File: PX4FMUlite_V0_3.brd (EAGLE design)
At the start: 48.6 x 34.9 mm, 152 parts, among them J2 DF13-4P-1.25V, J201 DF13C-6P-1.25V, J202 DF13C-6P-1.25V, J203 DF13C-6P-1.25V, J3 DF13C-4P-1.25V, J302 DF13C-4P-1.25V, J401 DF13C-4P-1.25V, J403 DF13C-7P-1.25V, J405 DF13C-4P-1.25V, J801 JST-ZH-3, J802 DF13C-3P-1.25V, M3_MOUNT1101 MOUNT-HOLE3.1MM, M3_MOUNT1102 MOUNT-HOLE3.1MM, M3_MOUNT1103 MOUNT-HOLE3.1MM, M3_MOUNT1104 MOUNT-HOLE3.1MM, U101 STM32F4X7VX, U2 MAX3051, U401 MAX3051, U903 74LVC2G240, X101 3.2x2.5 mm / 24 MHz / 15 ppm

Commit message: More tweaks
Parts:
- moved U$202 0.41 mm to (32.9, 7.52), turned to 180 degrees
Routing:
- net SERIAL2_TX: track 0.00 -> 6.91 mm
- net SERIAL2_RX: track 0.00 -> 5.37 mm
- net SERIAL2_CTS: track 0.00 -> 4.00 mm
- net 5V_S2_FILTERED: track 16.2 -> 18.7 mm
- net SERIAL2_RTS: track 0.00 -> 2.41 mm
- net VDD_5V_PERIPH: track 0.00 -> 2.28 mm, vias 0 -> 2
- net VDD_5V: track 14.7 -> 16.7 mm, vias 0 -> 4
- net N$5: track 0.00 -> 1.30 mm, vias 5 -> 0
- net GND: track 109.3 -> 110.5 mm, vias 9 -> 23
- net VDD_IN: track 67.6 -> 68.4 mm

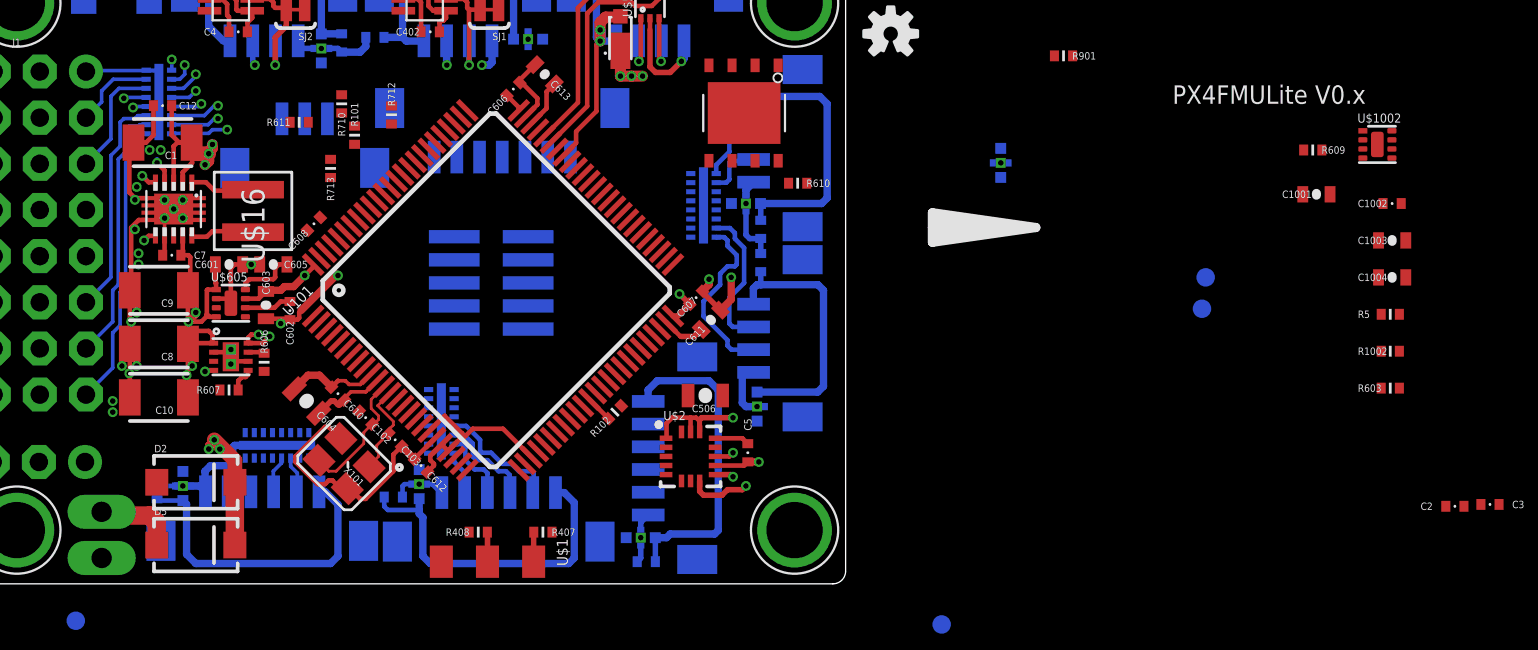
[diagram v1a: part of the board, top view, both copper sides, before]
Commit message: More wiring of peripheral 5V power
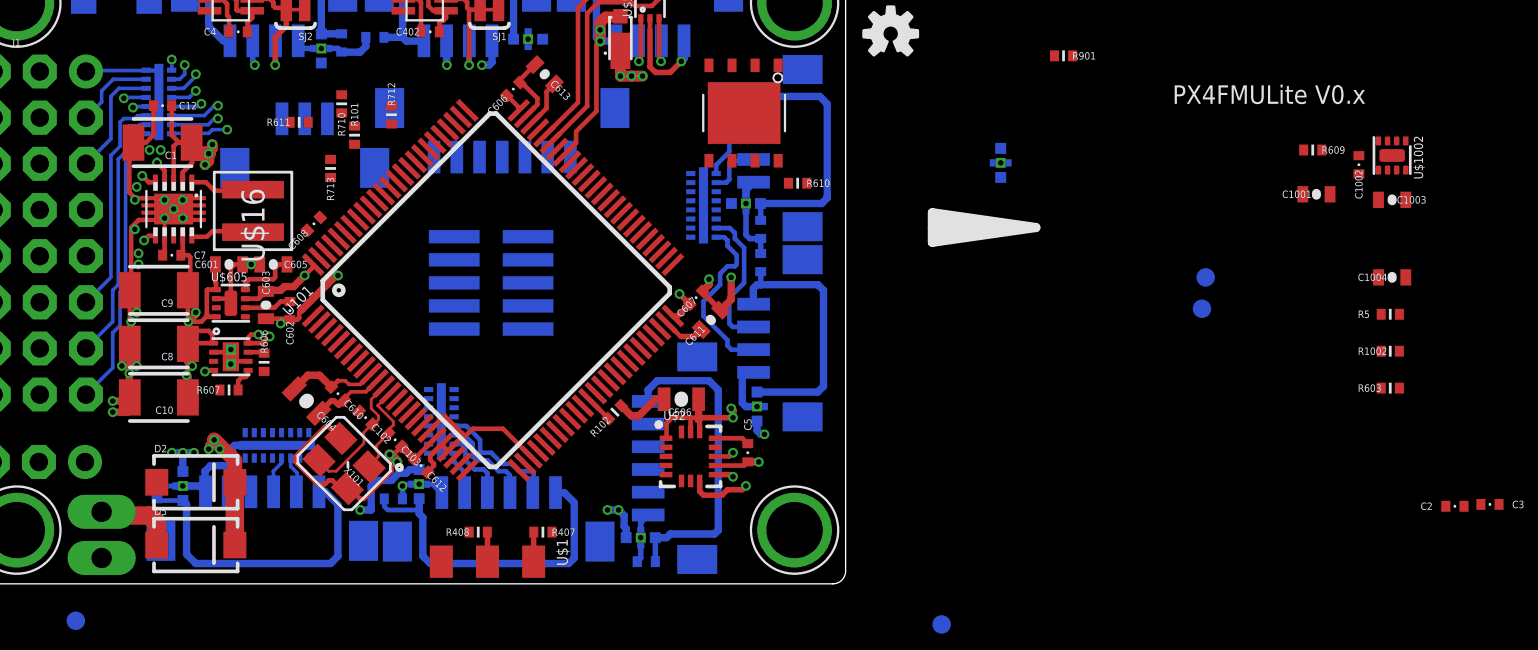
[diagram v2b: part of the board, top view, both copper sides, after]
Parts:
- moved C1002 2.81 mm to (86.1, 25.8), turned to 90 degrees
- moved C1003 2.24 mm to (87.9, 23.9), turned to 180 degrees
- moved C506 1.34 mm to (48.8, 12.9)
- moved U$1002 1.02 mm to (87.9, 26.3), turned to 270 degrees
- moved U$202 0.10 mm to (32.9, 7.42)
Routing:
- net VDD_5V_PERIPH: track 2.28 -> 65.1 mm, vias 2 -> 9
- net GND: track 110.5 -> 119.1 mm, vias 23 -> 26
- net VDD_5V: track 16.7 -> 19.2 mm
- net VDD_3V3_SENSORS: track 7.20 -> 9.48 mm, vias 1 -> 2
- net VDD_IN: track 68.4 -> 67.4 mm

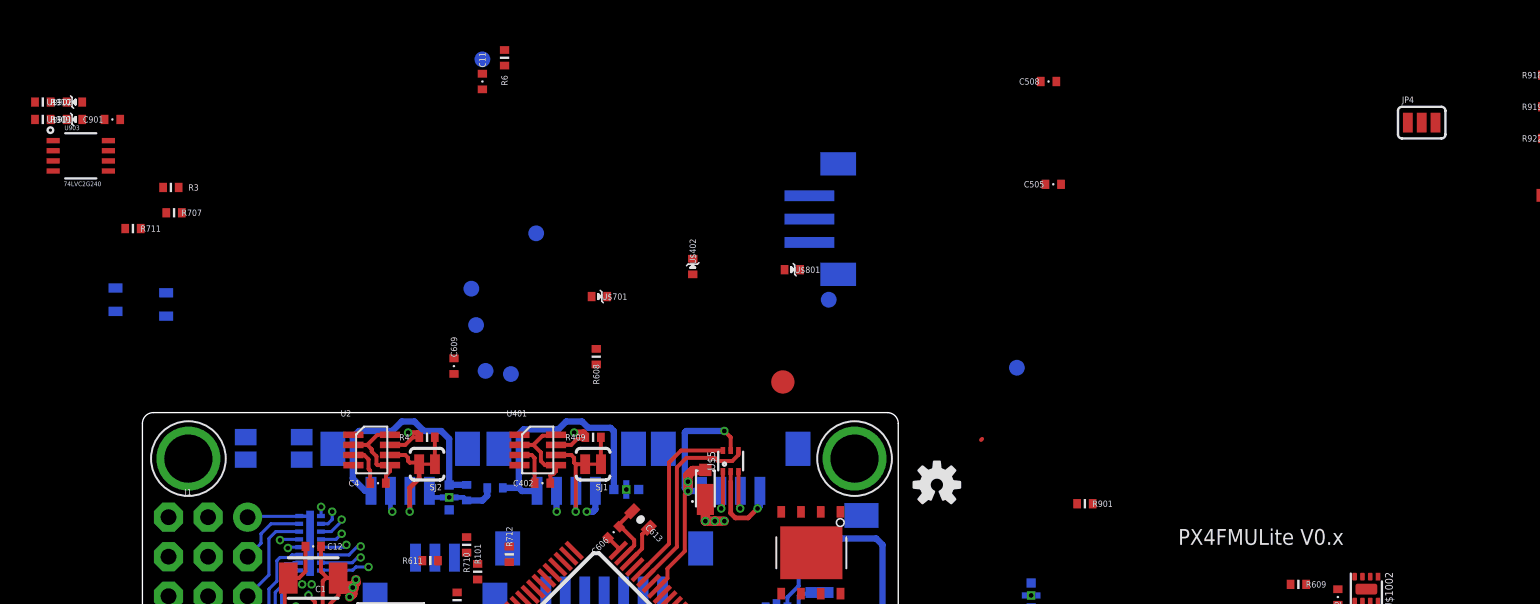
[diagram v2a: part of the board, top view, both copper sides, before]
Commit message: Removed SBUS interface that would not fit
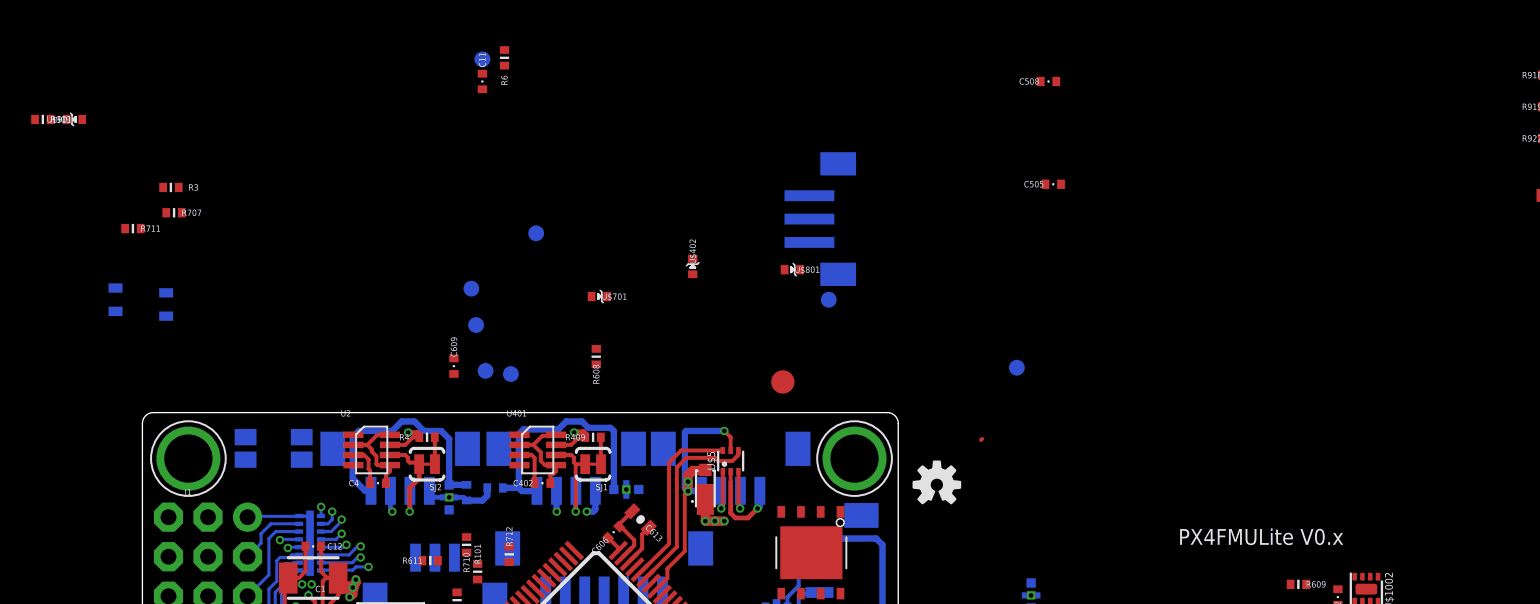
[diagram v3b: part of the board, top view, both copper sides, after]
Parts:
- removed C901: 0u1, pixhawk2:0402-CAP
- removed JP4: JUMPER-3SMD, SparkFun-Passives:SJ_3
- removed R901: 10K, pixhawk2:0402-RES
- removed R910: 220R, pixhawk2:0402-RES
- removed U$902: PESD0402-140, pixhawk2:0402-TVS
- removed U903: 74LVC2G240, pixhawk2:TSSOP8_SOT505-2
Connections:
- removed net !SBUS_OUTPUT_EN: U903.7
- removed net N$38: R901.P$2, R910.P$1, U$902.C, U903.3
- removed net N$99: R910.P$2
- removed net RSSI_IN: R901.P$1
- removed net SBUS_INPUT: U903.6
- removed net SBUS_OUTPUT: U903.5
- net GND: no longer C901.P$2, U$902.A, U903.1, U903.4
- net PPM_INPUT: no longer U903.2
- net VDD_3V3_PERIPH: no longer C901.P$1, U903.8
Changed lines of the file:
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@@
 <attribute name="PARTNO" value="RC0402FR-07470RL" x="30.7848" y="27.432" size="1.778" layer="27" rot="R270" display="off"/>
-</element>
-<element name="U903" library="pixhawk2" package="TSSOP8_SOT505-2" value="74LVC2G240" x="5.2832" y="54.1528" rot="R270">
-<attribute name="PARTNO" value="74LVC2G240DP,125" x="5.2832" y="54.1528" size="1.778" layer="27" rot="R270" display="off"/>
-</element>
-<element name="R901" library="pixhawk2" package="0402-RES" value="10K" x="69.7992" y="31.8008" rot="R180">
-<attribute name="PARTNO" value="RC0402FR-0710KL" x="69.799196875" y="31.394403125" size="1.778" layer="27" rot="R180" display="off"/>
 </element>
 <element name="R607" library="pixhawk2" package="0402-RES" value="10K" x="23.876" y="13.4112">
 <attribute name="PARTNO" value="RC0402FR-0710KL" x="23.876" y="13.4112" size="1.778" layer="27" display="off"/>
 </element>
-<element name="C901" library="pixhawk2" package="0402-CAP" value="0u1" x="7.3152" y="56.4896">
-<attribute name="PARTNO" value="CC0402ZRY5V7BB104" x="7.3152" y="56.4896" size="1.778" layer="27" display="off"/>
-</element>
 <element name="L201" library="pixhawk2" package="KYOCERA-KNH16-DA" value="KNH16C104DA5TS" x="46.5328" y="5.2832" rot="MR180">
 <attribute name="PARTNO" value="KNH16C104DA5TS" x="46.5328" y="5.2832" size="1.778" layer="28" rot="MR180" display="off"/>
@@
 <attribute name="PARTNO" value="RC0402FR-07220RL" x="2.8448" y="56.4896" size="1.778" layer="27" rot="R180" display="off"/>
 </element>
-<element name="R910" library="pixhawk2" package="0402-RES" value="220R" x="2.8448" y="57.6072" rot="R180">
-<attribute name="PARTNO" value="RC0402FR-07220RL" x="2.8448" y="57.6072" size="1.778" layer="27" rot="R180" display="off"/>
-</element>
 <element name="U$605" library="pixhawk2" package="MLF-8-EPAD" value="MIC5332" x="23.9776" y="18.1864">
 <attribute name="PARTNO" value="MIC5332-SSYMT" x="23.9776" y="18.1864" size="1.778" layer="27" display="off"/>
@@
 <element name="U$901" library="pixhawk2" package="0402-TVS" value="PESD0402-140" x="4.8768" y="56.4896">
 <attribute name="PARTNO" value="PESD0402-140" x="4.8768" y="56.4896" size="1.778" layer="27" display="off"/>
-</element>
-<element name="U$902" library="pixhawk2" package="0402-TVS" value="PESD0402-140" x="4.8768" y="57.6072">
-<attribute name="PARTNO" value="PESD0402-140" x="4.8768" y="57.6072" size="1.778" layer="27" display="off"/>
 </element>
 <element name="C604" library="pixhawk2" package="0805-CAP" value="10u/10V" x="28.1432" y="12.8016" rot="R135">
@@
 <element name="D2" library="SparkFun-DiscreteSemi" package="SMA-DIODE" value="B340A" x="22.0472" y="8.3312"/>
 <element name="D5" library="SparkFun-DiscreteSemi" package="SMA-DIODE" value="B340A" x="22.0472" y="4.8768"/>
-<element name="JP4" library="SparkFun-Passives" package="SJ_3" value="JUMPER-3SMD" x="91.44" y="56.2864"/>
 <element name="U$15" library="PX4lite" package="PWSON10" value="TPS6303X" x="20.828" y="23.368" rot="R180"/>
 <element name="U$16" library="ti_tps_soln2" package="XFL4020" value="XFL4020-222MEB" x="25.1968" y="23.2664" rot="R90">
@@
 <wire x1="47.5971875" y1="16.776278125" x2="49.2872" y2="21.8212" width="0" layer="19" extent="1-16"/>
 </signal>
-<signal name="SBUS_INPUT">
-<contactref element="U903" pad="6"/>
-</signal>
 <signal name="SAFETY">
 <contactref element="R713" pad="P$1"/>
@@
 </signal>
 <signal name="PPM_INPUT">
-<contactref element="U903" pad="2"/>
 <contactref element="R909" pad="P$1"/>
 <contactref element="U$901" pad="C"/>
 <wire x1="4.3768" y1="56.4896" x2="3.3448" y2="56.4896" width="0" layer="19" extent="1-1"/>
-<wire x1="3.5082" y1="54.4778" x2="3.3448" y2="56.4896" width="0" layer="19" extent="1-1"/>
-</signal>
-<signal name="SBUS_OUTPUT">
-<contactref element="U903" pad="5"/>
-</signal>
-<signal name="N$38">
-<contactref element="U903" pad="3"/>
-<contactref element="R901" pad="P$2"/>
-<contactref element="R910" pad="P$1"/>
-<contactref element="U$902" pad="C"/>
-<wire x1="3.5082" y1="53.8278" x2="69.2992" y2="31.8008" width="0" layer="19" extent="1-1"/>
-<wire x1="3.3448" y1="57.6072" x2="3.5082" y2="53.8278" width="0" layer="19" extent="1-1"/>
-<wire x1="4.3768" y1="57.6072" x2="3.3448" y2="57.6072" width="0" layer="19" extent="1-1"/>
 </signal>
 <signal name="N$57">
@@
 <contactref element="R407" pad="P$1"/>
 <wire x1="41.648" y1="5.588" x2="42.293884375" y2="11.472978125" width="0" layer="19" extent="1-1"/>
-</signal>
-<signal name="RSSI_IN">
-<contactref element="R901" pad="P$1"/>
-</signal>
-<signal name="!SBUS_OUTPUT_EN">
-<contactref element="U903" pad="7"/>
 </signal>
 <signal name="N$68">
@@
 <signal name="PPM-SBUS-PROT">
 <contactref element="R909" pad="P$2"/>
-</signal>
-<signal name="N$99">
-<contactref element="R910" pad="P$2"/>
 </signal>
 <signal name="VDD_3V3_SPEKTRUM" class="1">
@@
 <contactref element="U101" pad="20"/>
 <contactref element="C602" pad="P$1"/>
-<contactref element="U903" pad="4"/>
-<contactref element="U903" pad="1"/>
-<contactref element="C901" pad="P$2"/>
 <contactref element="J403" pad="P$7"/>
 <contactref element="L402" pad="P$3"/>
@@
 <contactref element="U$801" pad="A"/>
 <contactref element="U$901" pad="A"/>
-<contactref element="U$902" pad="A"/>
 <contactref element="C604" pad="P$2"/>
 <contactref element="GND" pad="P$1"/>
@@
 <wire x1="67.9624" y1="58.928" x2="68.2672" y2="52.324" width="0" layer="19" extent="1-1"/>
 <wire x1="9.136" y1="49.4792" x2="15.8784" y2="36.0818" width="0" layer="19" extent="1-16"/>
-<wire x1="3.5082" y1="53.1778" x2="9.136" y2="49.4792" width="0" layer="19" extent="1-1"/>
-<wire x1="3.5082" y1="55.1278" x2="3.5082" y2="53.1778" width="0" layer="19" extent="1-1"/>
-<wire x1="5.3768" y1="56.4896" x2="3.5082" y2="55.1278" width="0" layer="19" extent="1-1"/>
-<wire x1="5.3768" y1="57.6072" x2="5.3768" y2="56.4896" width="0" layer="19" extent="1-1"/>
-<wire x1="7.8152" y1="56.4896" x2="5.3768" y2="56.4896" width="0" layer="19" extent="1-1"/>
-<wire x1="16.3656" y1="66.6496" x2="7.8152" y2="56.4896" width="0" layer="19" extent="1-1"/>
+<wire x1="5.3768" y1="56.4896" x2="9.136" y2="49.4792" width="0" layer="19" extent="1-1"/>
+<wire x1="16.3656" y1="66.6496" x2="5.3768" y2="56.4896" width="0" layer="19" extent="1-1"/>
 <wire x1="31.0896" y1="58.428" x2="38.108" y2="45.1104" width="0" layer="19" extent="1-1"/>
 <wire x1="31.0896" y1="60.3504" x2="31.0896" y2="58.428" width="0" layer="19" extent="1-16"/>
@@
 </signal>
 <signal name="VDD_3V3_PERIPH" class="1">
-<contactref element="U903" pad="8"/>
-<contactref element="C901" pad="P$1"/>
 <contactref element="C1004" pad="P$1"/>
 <contactref element="U$1002" pad="7"/>
 <wire x1="87.134" y1="19.6088" x2="88.134" y2="25.5144" width="0" layer="19" extent="1-1"/>
-<wire x1="7.0582" y1="55.1278" x2="88.134" y2="25.5144" width="0" layer="19" extent="1-1"/>
-<wire x1="6.8152" y1="56.4896" x2="7.0582" y2="55.1278" width="0" layer="19" extent="1-1"/>
 </signal>
 <signal name="N$3">

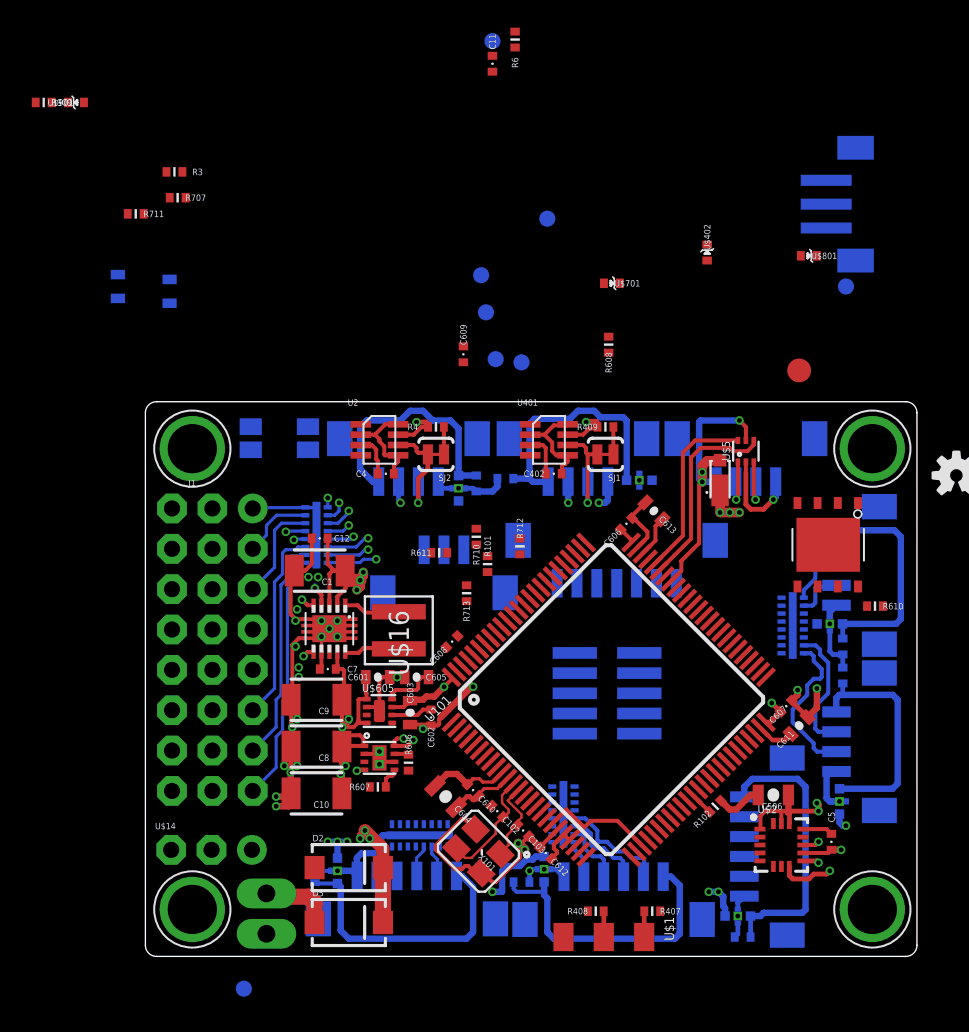
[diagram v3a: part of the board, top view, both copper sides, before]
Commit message: Reworked PPM and spektrum through ESD/filter
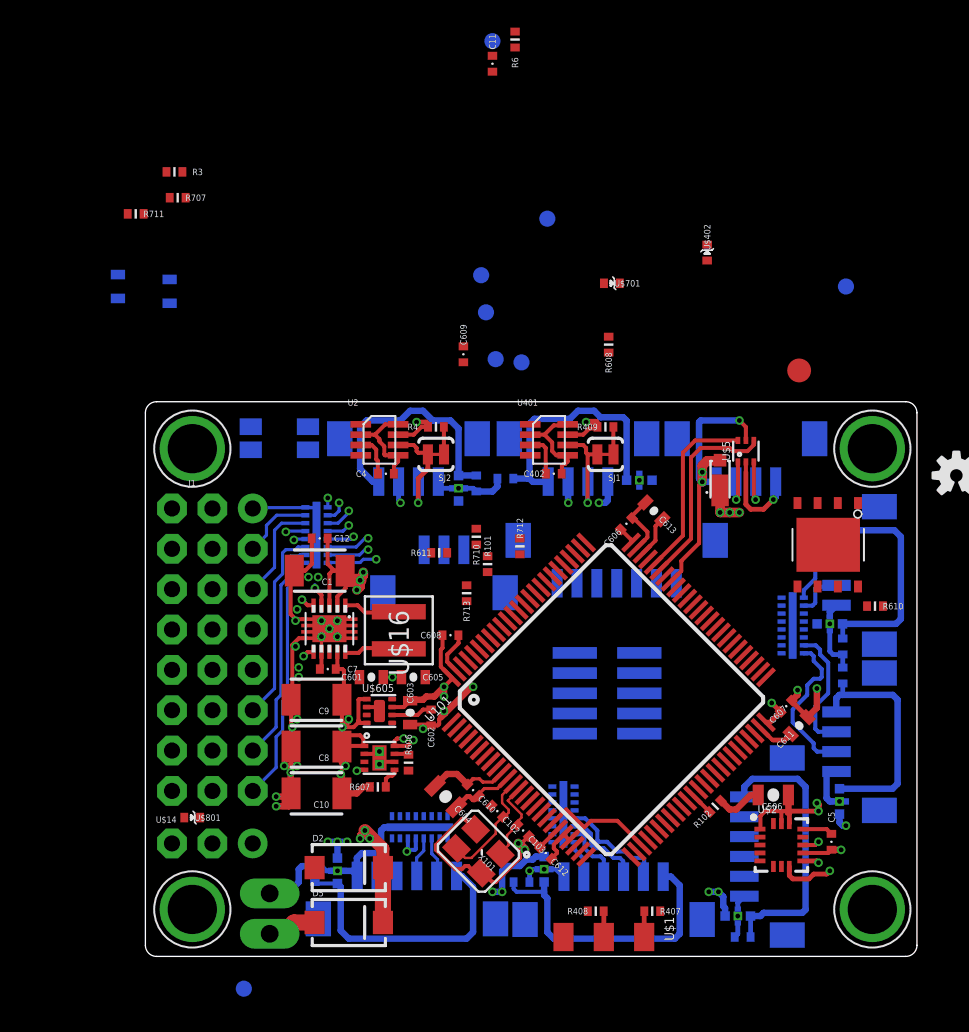
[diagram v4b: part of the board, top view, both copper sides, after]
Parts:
- removed J801: JST-ZH-3, for-transfers:JST-ZH-SMT-VERTICAL
- removed R909: 220R, pixhawk2:0402-RES
- removed U$901: PESD0402-140, pixhawk2:0402-TVS
- moved U$801 52.5 mm to (12.2, 11.5)
- moved JP5 2.55 mm to (17.1, 4.17), turned to 90 degrees
- moved L3 0.51 mm to (26.5, 10.9)
- moved C608 0.42 mm to (28.4, 23.0), turned to 0 degrees
- moved U$14 0.41 mm to (10.9, 9.86)
- moved C601 0.41 mm to (23.5, 20.3)
- moved C605 0.20 mm to (26.1, 20.3)
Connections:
- removed net PPM-SBUS-PROT: R909.P$2
- removed net PPM_INPUT: R909.P$1, U$901.C
- new net N$18: L3.P$13, L3.P$14, U$14.1
- net GND: now also U$14.3; no longer J801.P$2, U$901.A
- net IO-USART1_RX: now also L3.P$4; no longer J801.P$3
- net VDD_3V3_SPEKTRUM: now also U$14.2; no longer J801.P$1
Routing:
- net N$18: track 0.00 -> 15.5 mm, vias 0 -> 1
- net FMU-VDD_3V3: track 29.1 -> 32.9 mm, vias 2 -> 3
- net GND: track 119.1 -> 122.7 mm, vias 26 -> 27
- net VDD_3V3_SPEKTRUM: track 3.37 -> 0.00 mm
- net V_EXT: track 4.51 -> 3.12 mm
- net SERIAL3_TX: track 2.03 -> 2.54 mm
- net SERIAL3_RX: track 2.05 -> 2.56 mm
- net VDD_5V_PERIPH: track 65.1 -> 64.9 mm, vias 9 -> 10
